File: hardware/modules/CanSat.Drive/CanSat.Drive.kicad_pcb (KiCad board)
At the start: 2 copper layers, 60 x 40 mm, 49 parts, among them J101 Conn_01x02_Pin, J102 Conn_01x02_Pin, J301 Conn_01x04_MountingPin, J401 Conn_01x04_MountingPin, J501 Conn_01x02_Pin, J502 Conn_01x02_Pin, Q101 Q_NMOS_DGS, SW201 RESET_sw, U201 TPS3820, U202 SN65HVD230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

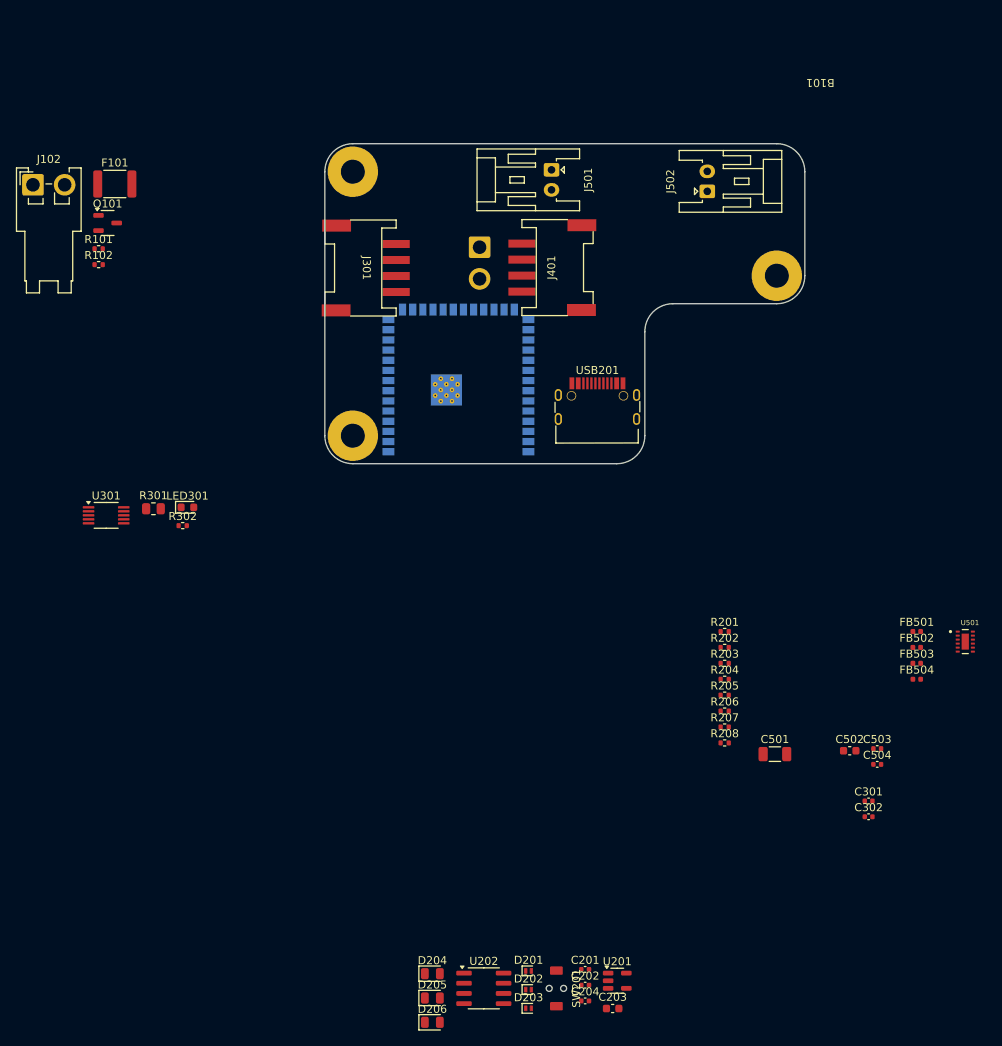
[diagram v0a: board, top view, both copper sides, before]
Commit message: 2/3配線
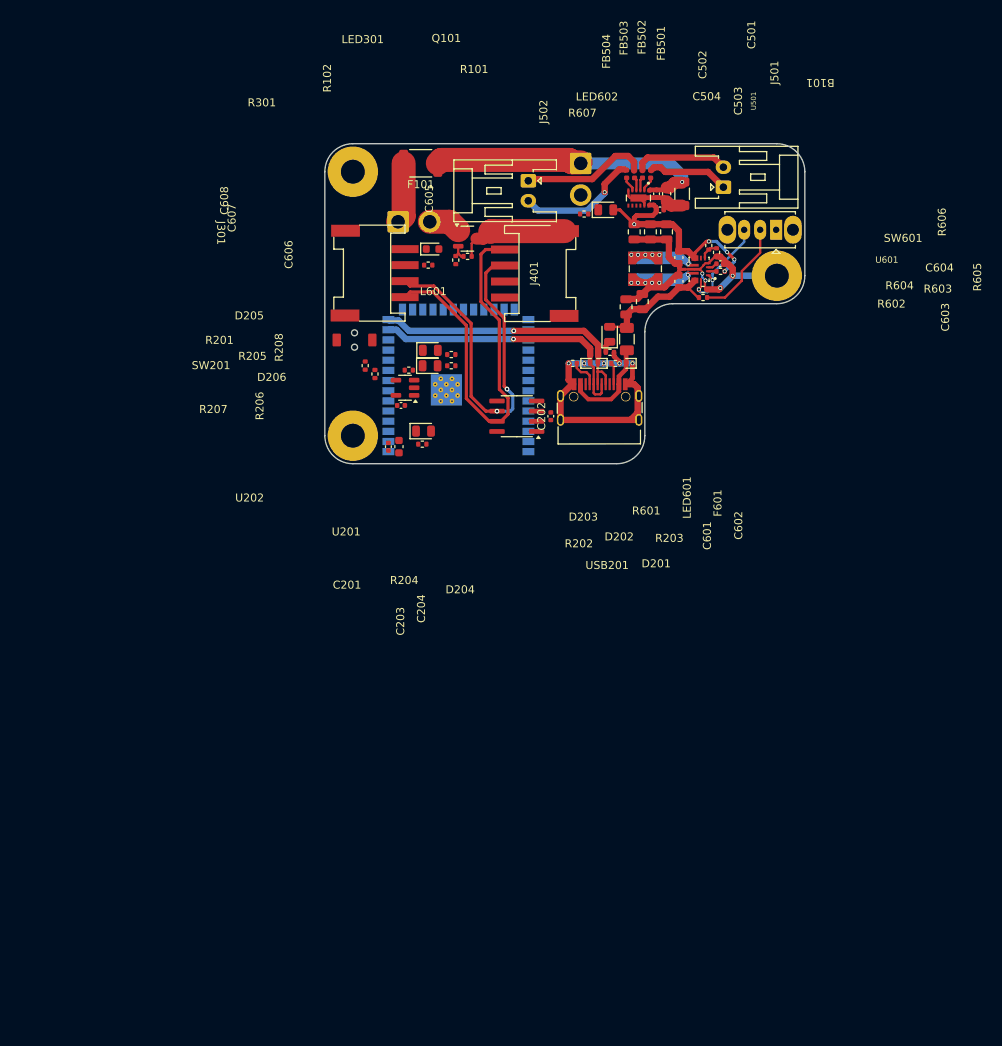
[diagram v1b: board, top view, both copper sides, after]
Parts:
- removed C301, C302: 100nF, Capacitor_SMD:C_0402_1005Metric
- removed the R301 at (93.2, 116.4)
- removed U301: INA226, Package_SO:VSSOP-10_3x3mm_P0.5mm
- added C601: 22uF, Capacitor_SMD:C_0805_2012Metric, F.Cu at (152.3, 91.2)
- added C602: 22uF, Capacitor_SMD:C_0805_2012Metric, F.Cu at (154.3, 90.5)
- added C603: 10uF, Capacitor_SMD:C_0603_1608Metric, F.Cu at (158.9, 88.0)
- added C604: 100nF, Capacitor_SMD:C_0402_1005Metric, F.Cu at (164.1, 85.8)
- added C605: 10uF, Capacitor_SMD:C_0603_1608Metric, F.Cu at (158.9, 85.0)
- added C606: 22uF, Capacitor_SMD:C_0805_2012Metric, F.Cu at (157.3, 81.8)
- added C607: 22uF, Capacitor_SMD:C_0805_2012Metric, F.Cu at (155.3, 81.8)
- added C608: 22uF, Capacitor_SMD:C_0805_2012Metric, F.Cu at (153.3, 81.8)
- added F601: Polyfuse, Fuse:Fuse_1206_3216Metric, F.Cu at (152.4, 95.2)
- added L601: L, Inductor_SMD:L_Wuerth_WE-TPC-3816, F.Cu at (154.7, 86.4)
- added LED601: USB Power, LED_SMD:LED_0805_2012Metric, F.Cu at (150.2, 94.6)
- added LED602: VDD, LED_SMD:LED_0805_2012Metric, F.Cu at (149.7, 79.0)
- added R601: 1k, Resistor_SMD:R_0402_1005Metric, F.Cu at (150.3, 96.8)
- added R602: 10k, Resistor_SMD:R_0402_1005Metric, F.Cu at (161.9, 90.0)
- added R603: 330k, Resistor_SMD:R_0402_1005Metric, F.Cu at (161.9, 89.0)
- added R604: 100k, Resistor_SMD:R_0402_1005Metric, F.Cu at (164.1, 86.7)
- added R605: 15k, Resistor_SMD:R_0402_1005Metric, F.Cu at (163.6, 84.4)
- added R606: 47k, Resistor_SMD:R_0402_1005Metric, F.Cu at (162.6, 83.5)
- added R607: 1k, Resistor_SMD:R_0402_1005Metric, F.Cu at (147.0, 79.6)
- added SW601: Power Switch, Button_Switch_THT:SW_Slide_SPDT_Straight_CK_OS102011MS2Q, F.Cu at (171.0, 81.5)
- added U601: TPS63070RNMR, WOBCLibrary:VREG_TPS63070RNMR, F.Cu at (161.4, 86.5)
- J102: moved to B.Cu
- moved SW201 84.9 mm to (118.3, 95.3), turned to 90 degrees
- moved D206 82.1 mm to (127.8, 98.5)
- moved D205 81.0 mm to (127.8, 96.6)
- moved D203 81.0 mm to (147.4, 98.2)
- moved D202 78.8 mm to (149.1, 98.2), turned to 180 degrees
- moved U201 78.7 mm to (124.7, 101.3), turned to 180 degrees
- moved D201 77.0 mm to (152.7, 98.2), turned to 180 degrees
- moved C203 75.1 mm to (123.9, 108.6), turned to 90 degrees
- moved C503 74.6 mm to (156.1, 77.0), turned to -90 degrees
- moved C504 74.4 mm to (156.5, 79.0)
- moved C201 74.2 mm to (124.2, 103.5), turned to 180 degrees
- moved C204 73.5 mm to (122.6, 108.6), turned to -90 degrees
- moved C502 73.3 mm to (157.3, 77.0), turned to -90 degrees
- moved FB504 72.8 mm to (152.3, 74.6), turned to 90 degrees
- moved U202 71.6 mm to (138.6, 104.8), turned to 180 degrees
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- renumbered R302 to R301
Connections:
- J301 pad 3: Net-(J301-Pin_3) -> VDD
- R301 pad 2: Net-(J301-Pin_3) -> VDD
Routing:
- net GND: track 0.00 -> 100.8 mm, vias 0 -> 9
- net /CANH: track 0.00 -> 50.1 mm
- net /CANL: track 0.00 -> 46.9 mm, vias 0 -> 2
- net VM: track 0.00 -> 36.7 mm, vias 0 -> 1
- net /ESP32Core/USB_D+: track 0.00 -> 34.7 mm, vias 0 -> 1
- net /ESP32Core/USB_D-: track 0.00 -> 34.2 mm, vias 0 -> 1
- net VDD: track 0.00 -> 28.7 mm, vias 0 -> 5
- net VBUS: track 0.00 -> 22.6 mm
- net Net-(LED601-A): track 0.00 -> 16.1 mm
- net Net-(J502-Pin_1): track 0.00 -> 15.9 mm
- net Net-(J502-Pin_2): track 0.00 -> 15.7 mm, vias 0 -> 1
- net Net-(U601-L1): track 0.00 -> 15.7 mm, vias 0 -> 6
- net Net-(U601-L2): track 0.00 -> 15.4 mm, vias 0 -> 6
- net Net-(SW601-C): track 0.00 -> 13.1 mm, vias 0 -> 2
- net Net-(SW601-B): track 0.00 -> 12.5 mm
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
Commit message: 一旦
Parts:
- moved R301 0.65 mm to (128.1, 85.6), turned to -90 degrees
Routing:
- net GND: track 100.8 -> 161.2 mm, vias 9 -> 11
- net VDD: track 28.7 -> 60.2 mm, vias 5 -> 7
- net Net-(U201-MR): track 0.00 -> 7.95 mm
- net /SDA: track 0.00 -> 2.97 mm, vias 0 -> 1
- net /SCL: track 0.00 -> 1.70 mm, vias 0 -> 1
- net Net-(LED301-A): track 0.00 -> 1.49 mm
- net Net-(LED602-K): track 0.00 -> 1.47 mm
- net /ESP32Core/WDI: track 0.00 -> 0.96 mm, vias 0 -> 1

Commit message: デザインルールチェックまで完了
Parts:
- removed R206, R208: 10k, Resistor_SMD:R_0402_1005Metric
- added D601: 1N5819WS, Diode_SMD:D_SOD-323, F.Cu at (151.3, 81.7)
- added D602: 1N5819WS, Diode_SMD:D_SOD-323, F.Cu at (151.3, 85.0)
- moved J401 1.22 mm to (139.6, 87.2)
- moved USB201 0.17 mm to (148.8, 104.5)
- moved C601 0.15 mm to (152.1, 91.2)
- moved SW601 0.14 mm to (170.9, 81.6)
- moved C602 0.12 mm to (154.2, 90.5)
- moved R602 0.07 mm to (161.9, 89.9)
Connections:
- C605 pad 1: VDD -> Net-(D601-A2)
- C606 pad 1: VDD -> Net-(D601-A2)
- C607 pad 1: VDD -> Net-(D601-A2)
- C608 pad 1: VDD -> Net-(D601-A2)
- J301 pad 3: VDD -> VBATT+
- R102 pad 1: /ESP32Core/GPIO14 -> /ESP32Core/GPIO13
- R301 pad 2: VDD -> VBATT+
- R604 pad 1: VDD -> Net-(D601-A2)
- R606 pad 2: VDD -> Net-(D601-A2)
- U203 pad 10: /SDA -> /ESP32Core/I2C_SDA
- U203 pad 18: /AIN1 -> /ESP32Core/GPIO10/ADC1_CH9
- U203 pad 19: /AIN2 -> /ESP32Core/GPIO11
- U203 pad 20: /BIN1 -> /ESP32Core/GPIO12
- U203 pad 21: /BIN2 -> /ESP32Core/GPIO13
- U203 pad 22: /ESP32Core/GPIO14 -> /BIN2
- U203 pad 23: /ESP32Core/GPIO21 -> /BIN1
- U203 pad 24: /ESP32Core/GPIO47 -> /AIN2
- U203 pad 25: /ESP32Core/GPIO48 -> /AIN1
- U203 pad 9: /SCL -> /ESP32Core/I2C_SCL
- U601 pad 7_8: VDD -> Net-(D601-A2)
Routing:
- net GND: track 161.2 -> 305.2 mm, vias 11 -> 204
- net VBATT+: track 0.00 -> 27.8 mm, vias 0 -> 2
- net /BIN2: track 0.00 -> 27.4 mm, vias 0 -> 1
- net /BIN1: track 0.00 -> 27.1 mm, vias 0 -> 1
- net /AIN2: track 0.00 -> 26.8 mm, vias 0 -> 1
- net /AIN1: track 0.00 -> 26.3 mm, vias 0 -> 1
- net VDD: track 60.2 -> 83.9 mm, vias 7 -> 9
- net Net-(D601-A2): track 0.00 -> 22.0 mm, vias 0 -> 4
- net Net-(U203-MTMS/GPIO42): track 0.00 -> 12.1 mm, vias 0 -> 1
- net Net-(U203-MTDI/GPIO41/CLK_OUT1): track 0.00 -> 11.8 mm, vias 0 -> 1
- net RESET: track 0.00 -> 8.03 mm, vias 0 -> 1
- net /ESP32Core/GPIO13: track 0.00 -> 6.08 mm, vias 0 -> 1
- net /SDA: track 2.97 -> 0.00 mm, vias 1 -> 0
- net /ESP32Core/CAN_RX: track 0.00 -> 2.82 mm, vias 0 -> 1
- net /ESP32Core/CAN_TX: track 0.00 -> 2.58 mm, vias 0 -> 1
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- added copper zone on B.Cu, net GND
- added copper zone on F.Cu, net GND
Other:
- board text added: "CAN-C"
- board text added: "CAN-M"
- board text added: "Drive-Module created by WOBC"
- board text added: "ERROR"
- board text added: "ON"
- board text added: "RESET"
- board text added: "STAT"
- board text added: "VBUS"
- board text added: "VDD"

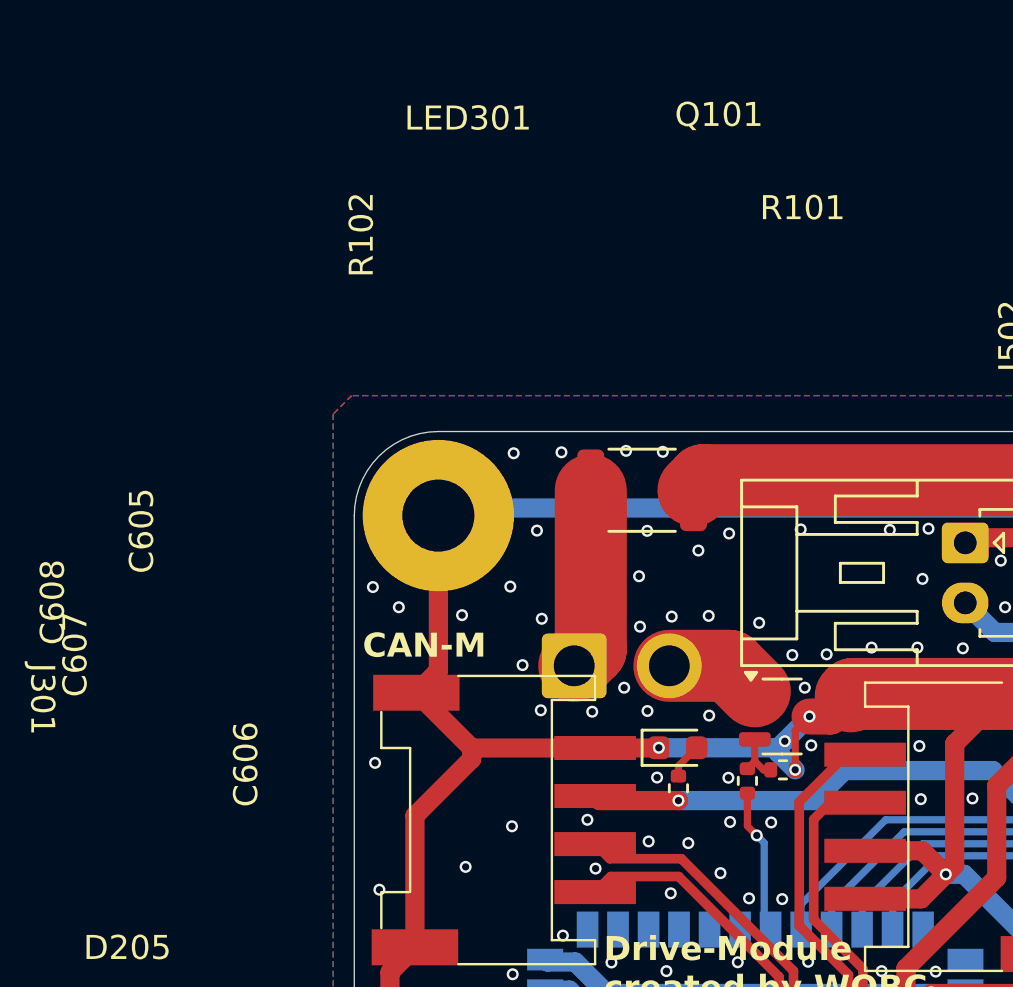
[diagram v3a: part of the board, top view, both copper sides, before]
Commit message: MOSFETの向きがおかしかったので修正
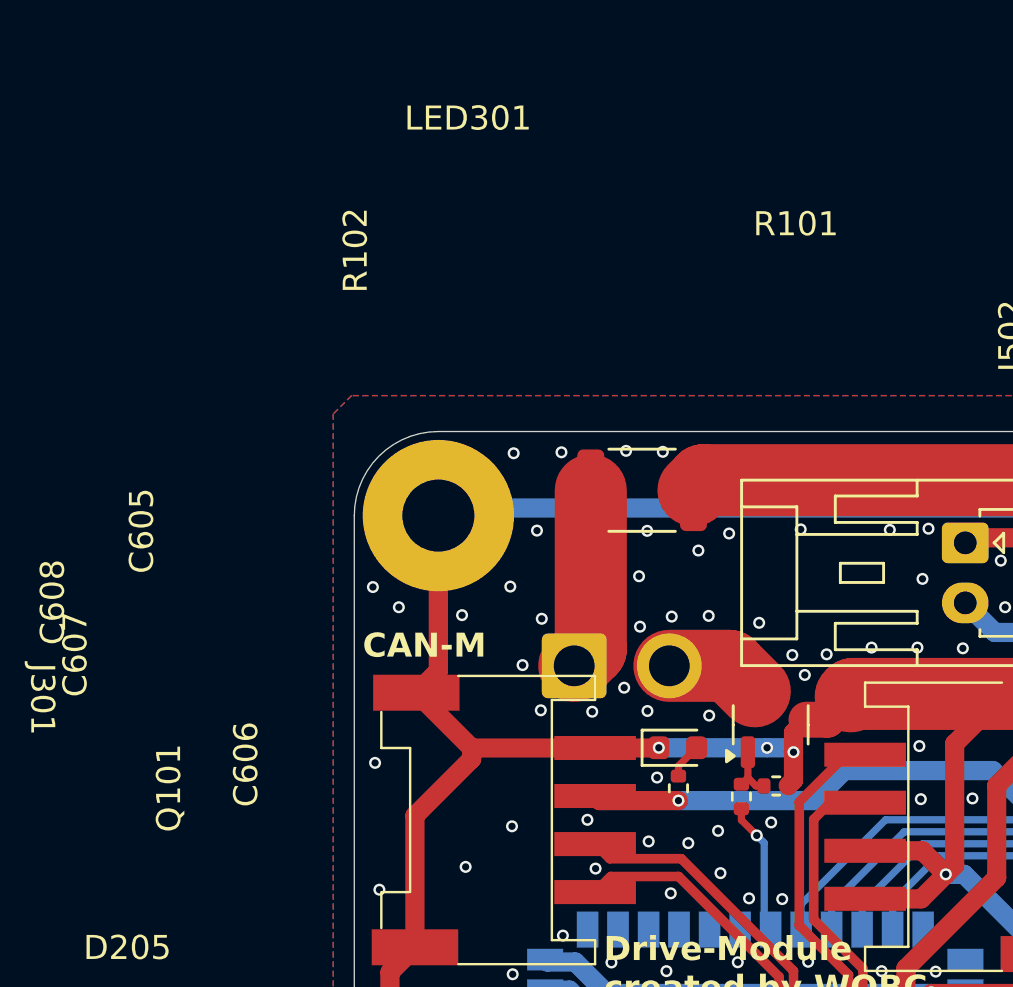
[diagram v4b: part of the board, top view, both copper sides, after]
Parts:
- moved R101 0.73 mm to (132.2, 85.5)
- moved R102 0.70 mm to (130.7, 86.0)
- moved Q101 0.59 mm to (132.0, 83.0), turned to 90 degrees
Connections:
- Q101 pad 1: Net-(J102-Pin_2) -> Net-(Q101-G)
- Q101 pad 2: Net-(Q101-G) -> GND
- Q101 pad 3: GND -> Net-(J102-Pin_2)
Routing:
- net GND: track 305.2 -> 303.6 mm, vias 204 -> 201

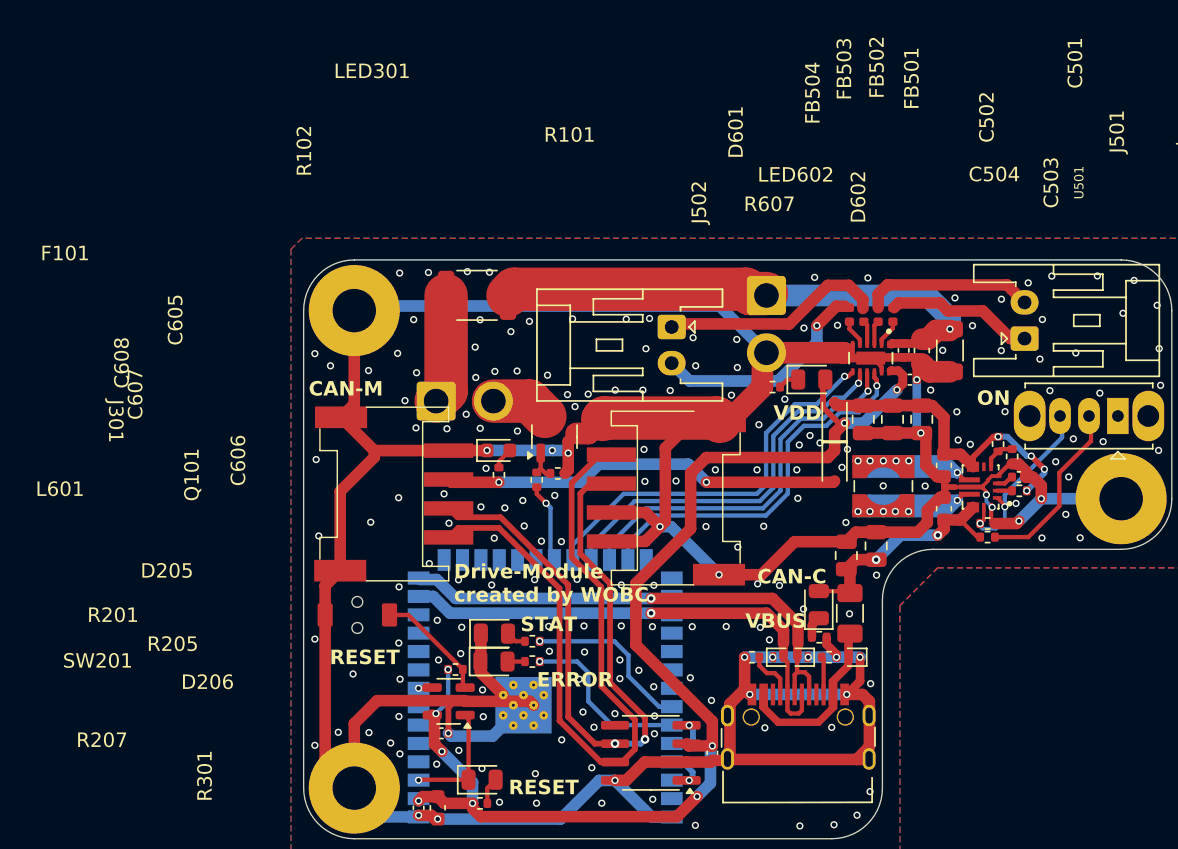
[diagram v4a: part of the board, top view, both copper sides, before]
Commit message: 100uFのコンデンサを25vt耐えられるものに変更，ガーバーファイル出力
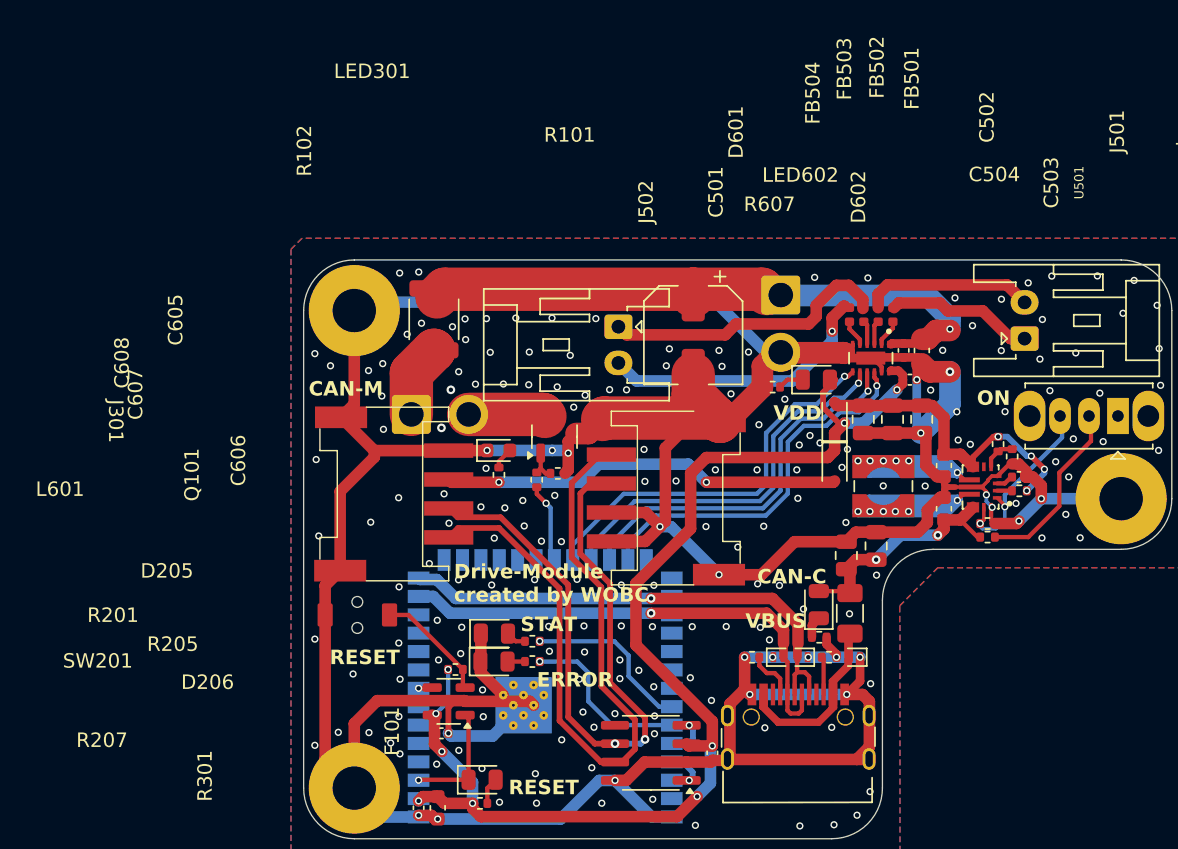
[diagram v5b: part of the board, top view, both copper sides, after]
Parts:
- C501: footprint Capacitor_SMD:C_1206_3216Metric -> Capacitor_SMD:CP_Elec_6.3x7.7
- moved C501 17.8 mm to (141.6, 76.0)
- moved J502 3.68 mm to (136.4, 75.4)
- moved F101 3.41 mm to (123.6, 74.9), turned to -90 degrees
- moved J102 1.94 mm to (122.1, 81.5)
- moved J101 0.99 mm to (147.6, 73.2)
- moved LED602 0.32 mm to (150.1, 79.0)
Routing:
- net GND: track 303.6 -> 312.5 mm, vias 201 -> 198
- net Net-(J502-Pin_1): track 15.4 -> 20.0 mm
- net VM: track 36.7 -> 41.2 mm
- net Net-(J502-Pin_2): track 15.7 -> 19.6 mm
- net Net-(J102-Pin_1): track 7.60 -> 5.08 mm
- net Net-(J102-Pin_2): track 4.00 -> 5.33 mm
- net VDD: track 83.9 -> 84.5 mm
